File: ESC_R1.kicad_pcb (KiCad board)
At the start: 4 copper layers, 174 parts, among them J101 Conn_01x03_Pin, J102 Conn_01x02_Pin, J103 Conn_01x02_Pin, J104 Conn_01x02_Pin, J201 Conn_01x05_Pin, J202 SWD TagConnect, J301 Conn_01x04_Male, J401 USB_C_Receptacle, Q501 BSC072N08NS5, Q502 BSC072N08NS5, Q601 BSC072N08NS5, Q602 BSC072N08NS5, Q701 BSC072N08NS5, Q702 BSC072N08NS5, SW201 PTS810 SJK, U101 TPS54332D, U102 TPS561208D, U103 TLV75533PDBV, U201 STM32F446RETx, U301 TJA1441AT, U401 USBLC6-2SC6, U501 IR2181S, U502 AD8418, U601 IR2181S, U602 AD8418, U701 IR2181S, U702 AD8418, Y201 16MHz

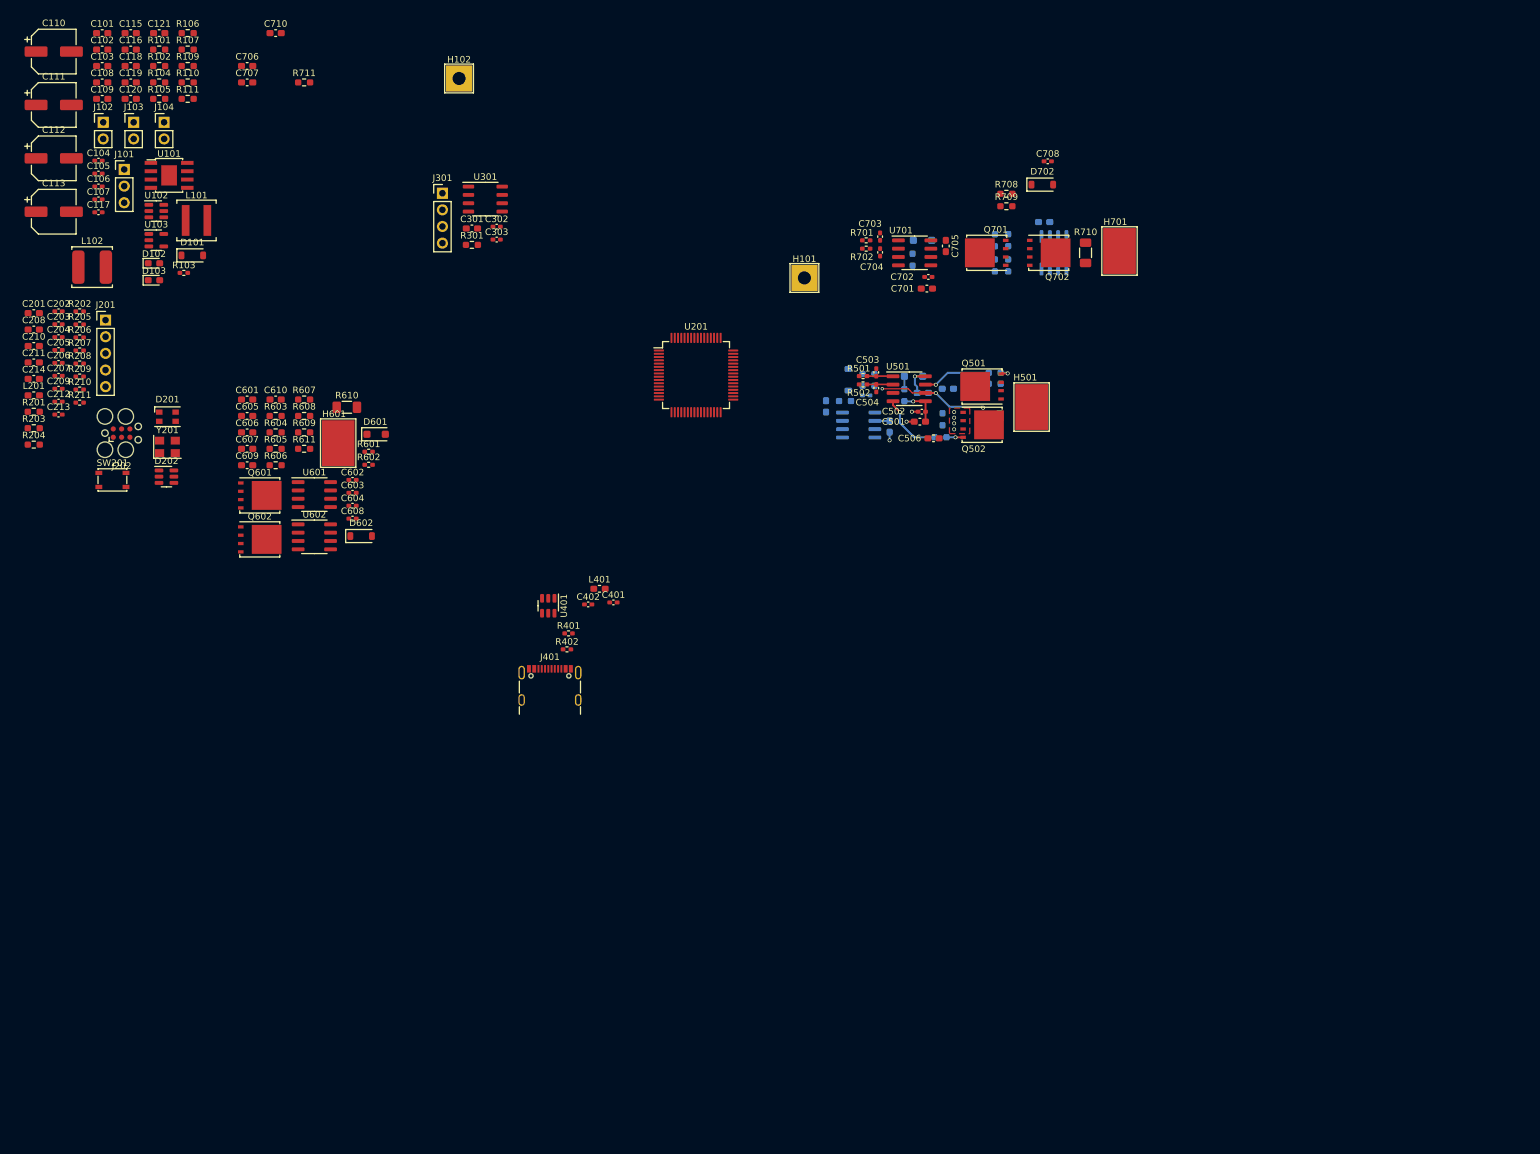
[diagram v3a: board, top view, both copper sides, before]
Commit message: feat: single phase, HSE, CAN routing and general layout
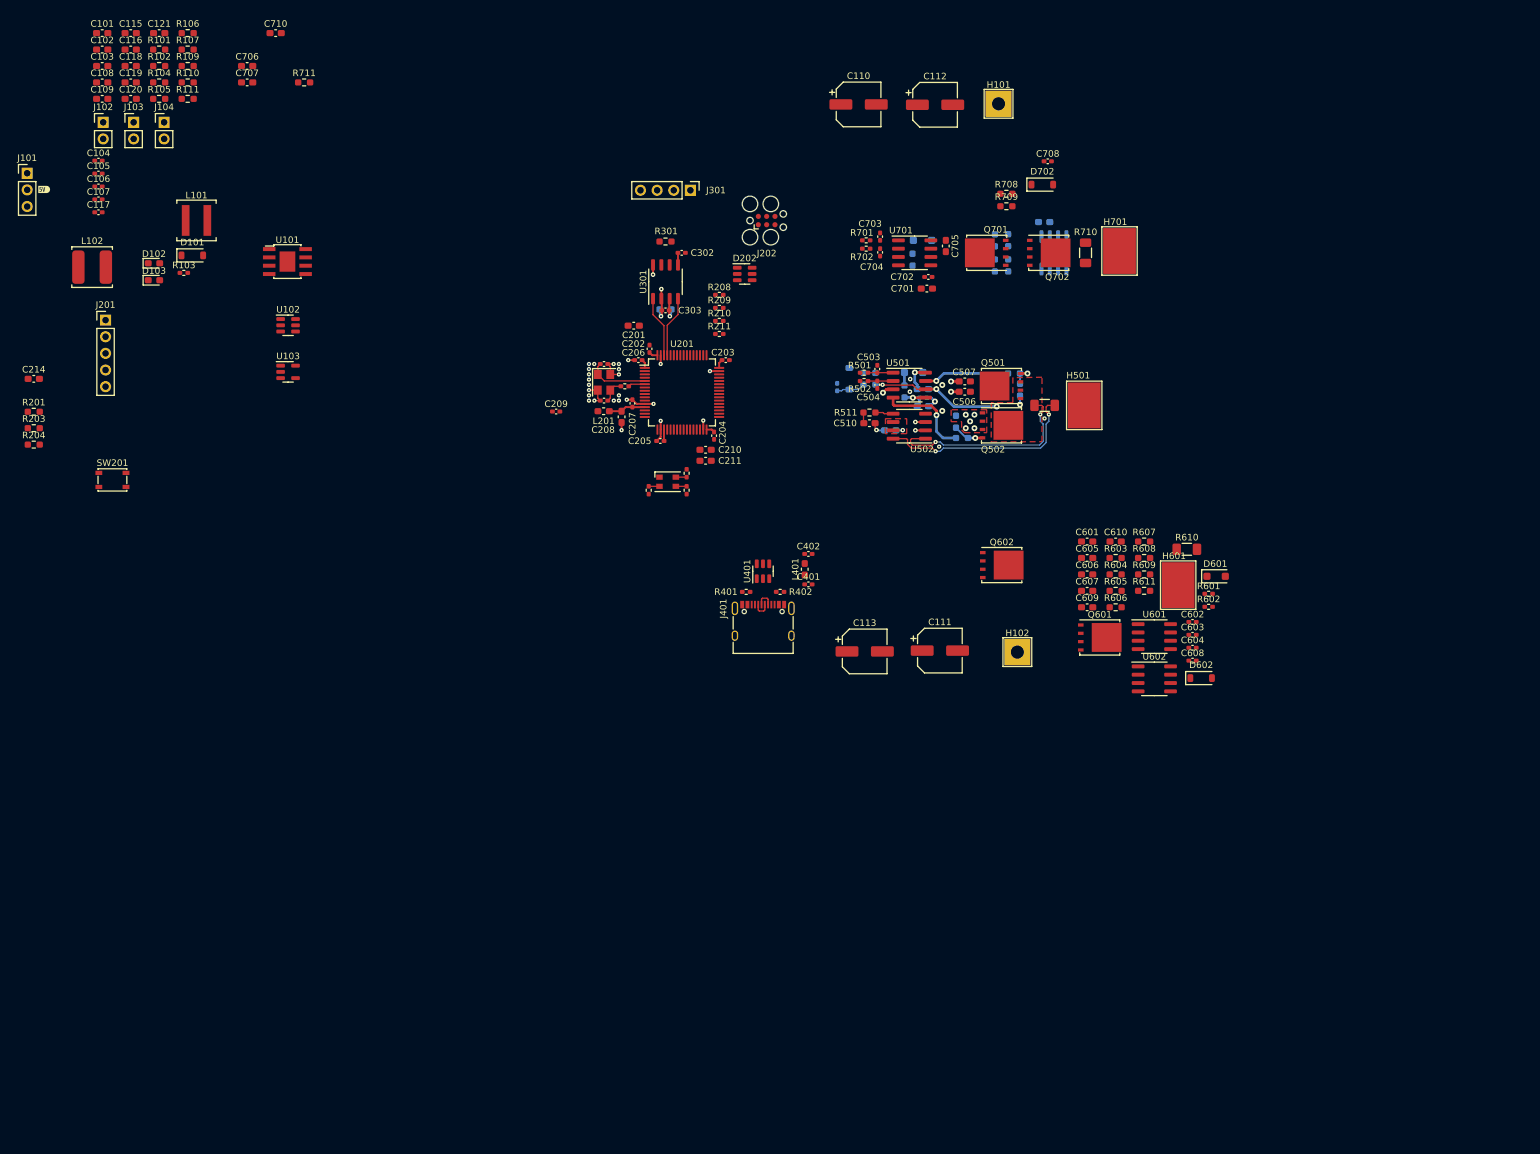
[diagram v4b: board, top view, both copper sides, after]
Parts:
- added kibuzzard-65860F08: G***, kibuzzard-65860F08, F.Cu at (18.3, 41.8)
- C301, C501, C502: moved to B.Cu
- C507, C510, R510, R511, U502: moved to F.Cu
- J401: footprint Connector_USB:USB_C_Receptacle_GCT_USB4105-xx-A_16P_TopMnt_Horizontal -> Connector_USB:USB_C_Receptacle_XKB_U262-16XN-4BVC11
- moved C111 158.9 mm to (155.0, 112.2)
- moved C113 140.8 mm to (143.6, 112.3)
- moved C112 134.8 mm to (154.3, 28.8)
- moved C601 130.1 mm to (177.5, 95.5)
- moved C602 130.1 mm to (193.6, 107.8)
- moved C603 130.1 mm to (193.6, 109.8)
- moved C604 130.1 mm to (193.6, 111.7)
- moved C605 130.1 mm to (177.5, 98.0)
- moved C606 130.1 mm to (177.5, 100.5)
- moved C607 130.1 mm to (177.5, 103.0)
- moved C608 130.1 mm to (193.6, 113.7)
- moved C609 130.1 mm to (177.5, 105.6)
- moved C610 130.1 mm to (181.9, 95.5)
- moved D601 130.1 mm to (197.2, 100.8)
- moved D602 130.1 mm to (194.9, 116.4)
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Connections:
- net /CAN/CANH renamed /CAN/CAN+
- net /CAN/CANL renamed /CAN/CAN-
- U401 pad 1: USB_D+ -> /USB/USB_CONN_D-
- U401 pad 3: USB_D- -> /USB/USB_CONN_D+
- U401 pad 4: /USB/USB_CONN_D- -> USB_D+
- U401 pad 6: /USB/USB_CONN_D+ -> USB_D-
- U502 pad 1: /3-Phase Bridge - Phase A/PHA_CIN- -> /3-Phase Bridge - Phase A/PHA_CIN+
- U502 pad 8: /3-Phase Bridge - Phase A/PHA_CIN+ -> /3-Phase Bridge - Phase A/PHA_CIN-
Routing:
- net GND: track 3.57 -> 41.1 mm, vias 3 -> 39
- net /3-Phase Bridge - Phase A/PHA_CIN+: track 17.7 -> 53.5 mm, vias 3 -> 6
- net /3-Phase Bridge - Phase A/PHA_CIN-: track 0.00 -> 32.3 mm, vias 0 -> 2
- net /MCU/HSE_IN: track 0.00 -> 9.34 mm
- net CAN_TXD: track 0.00 -> 9.33 mm
- net CAN_RXD: track 0.00 -> 9.32 mm
- net +3.3V: track 2.25 -> 10.0 mm, vias 0 -> 1
- net +3.3VA: track 0.00 -> 5.67 mm
- net /3-Phase Bridge - Phase A/PHA_LOUT: track 9.95 -> 14.6 mm
- net PHA_VSDIV: track 0.00 -> 4.41 mm
- net +5V: track 0.00 -> 3.87 mm, vias 0 -> 1
- net /MCU/XTAL_IN: track 0.00 -> 3.62 mm
- net /USB/USB_CONN_D+: track 0.00 -> 2.78 mm
- net /USB/USB_CONN_D-: track 0.00 -> 2.78 mm
- net PHA_C: track 0.00 -> 2.77 mm
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- added copper zone on F.Cu, net +3.3V
- added copper zone on F.Cu, net /3-Phase Bridge - Phase A/PHA_CIN+
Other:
- rule pad_to_mask_clearance: 0 -> 0.08

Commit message: feat: major circuit rework, style update and addition of a few extra subcomponents
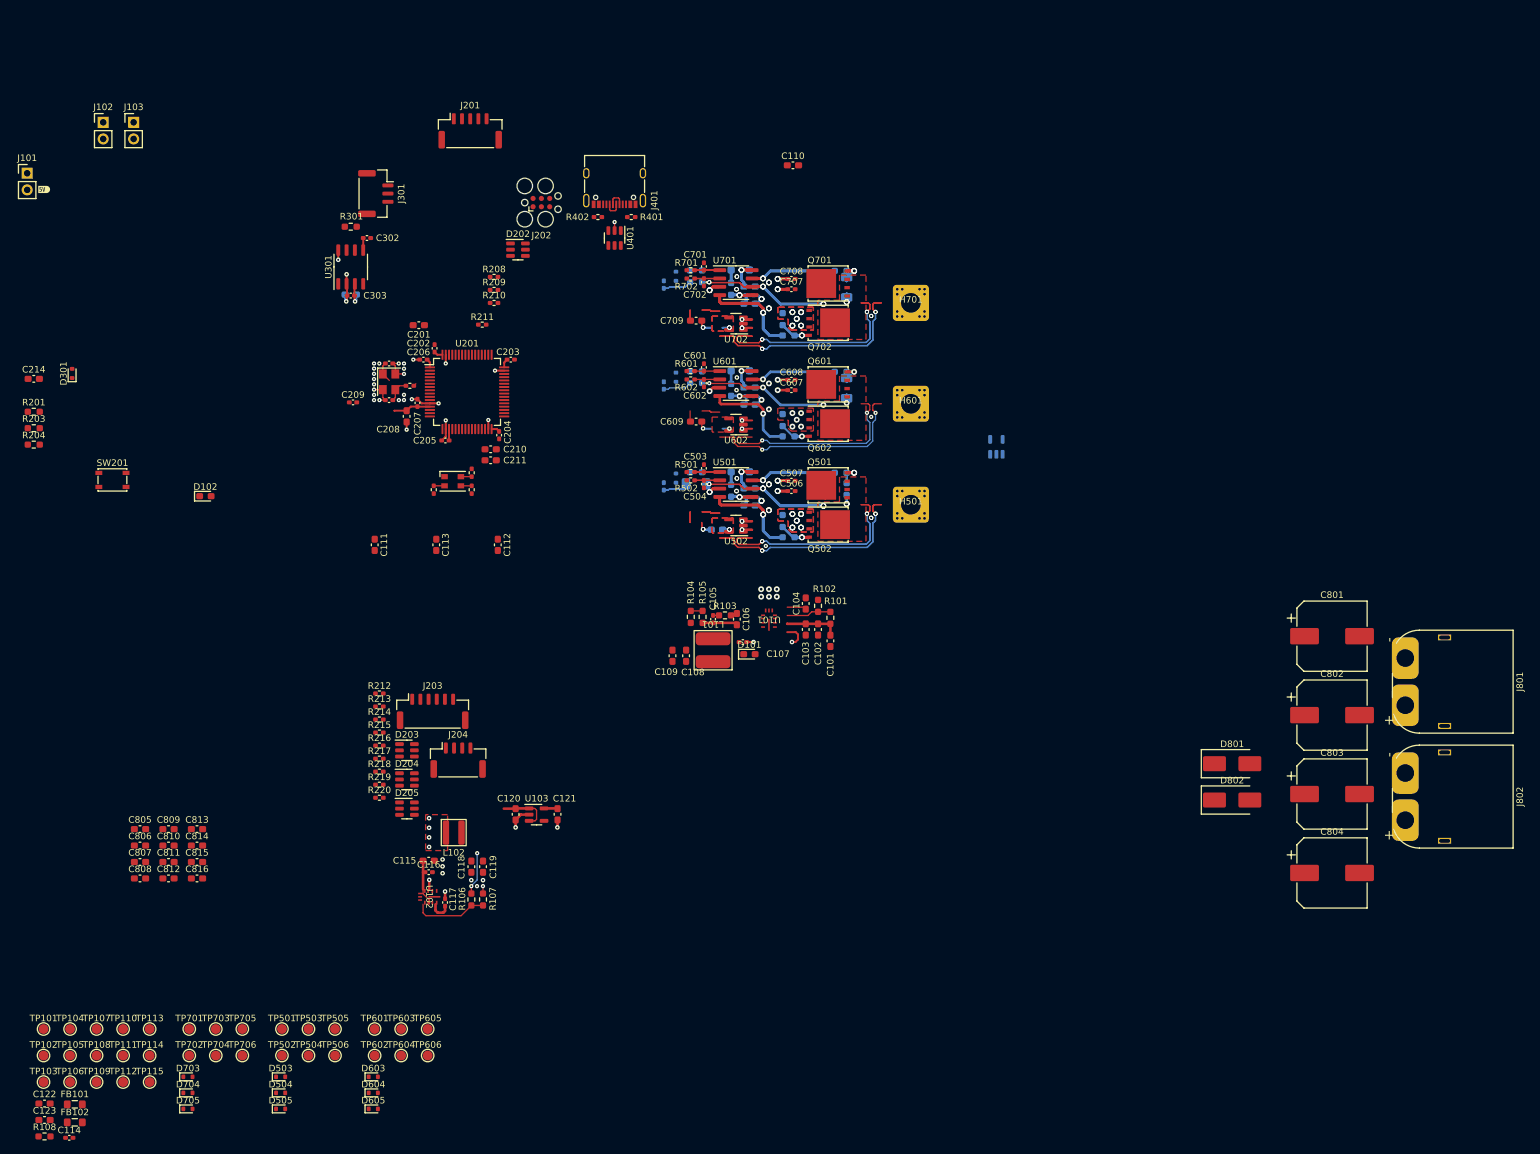
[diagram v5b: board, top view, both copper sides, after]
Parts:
- removed C401, C402: 100n, Capacitor_SMD:C_0402_1005Metric_Pad0.74x0.62mm_HandSolder
- removed C510, C610, C710: 10n, Capacitor_SMD:C_0603_1608Metric_Pad1.08x0.95mm_HandSolder
- removed D103: GREEN, LED_SMD:LED_0603_1608Metric_Pad1.05x0.95mm_HandSolder
- removed H101, H102: Pad, TestPoint:TestPoint_THTPad_4.0x4.0mm_Drill2.0mm
- removed J104: Conn_01x02_Pin, Connector_PinHeader_2.54mm:PinHeader_1x02_P2.54mm_Vertical
- removed L201, L401: WE742792625, Inductor_SMD:L_0603_1608Metric_Pad1.05x0.95mm_HandSolder
- removed R109: 0R5, Resistor_SMD:R_0603_1608Metric_Pad0.98x0.95mm_HandSolder
- removed R110: 1k, Resistor_SMD:R_0603_1608Metric_Pad0.98x0.95mm_HandSolder
- removed R111: 2k4, Resistor_SMD:R_0603_1608Metric_Pad0.98x0.95mm_HandSolder
- removed R510, R610, R710: 0.001, Resistor_SMD:R_1206_3216Metric_Pad1.30x1.75mm_HandSolder
- removed R511, R611, R711: 100, Resistor_SMD:R_0603_1608Metric_Pad0.98x0.95mm_HandSolder
- added C114: 100n 50V, Capacitor_SMD:C_0402_1005Metric_Pad0.74x0.62mm_HandSolder, F.Cu at (22.1, 186.6)
- added C122: 2u2 10V, Capacitor_SMD:C_0603_1608Metric_Pad1.08x0.95mm_HandSolder, F.Cu at (18.3, 181.3)
- added C123: 2u2 10V, Capacitor_SMD:C_0603_1608Metric_Pad1.08x0.95mm_HandSolder, F.Cu at (18.3, 183.8)
- added C801: 150u, Capacitor_SMD:CP_Elec_10x10.5, F.Cu at (214.9, 110.0)
- added C802: 150u, Capacitor_SMD:CP_Elec_10x10.5, F.Cu at (214.9, 122.0)
- added C803: 150u, Capacitor_SMD:CP_Elec_10x10.5, F.Cu at (214.9, 134.1)
- added C804: 150u, Capacitor_SMD:CP_Elec_10x10.5, F.Cu at (214.9, 146.1)
- added C805: 2u2 50V, Capacitor_SMD:C_0603_1608Metric_Pad1.08x0.95mm_HandSolder, F.Cu at (32.9, 139.4)
- added C806: 2u2 50V, Capacitor_SMD:C_0603_1608Metric_Pad1.08x0.95mm_HandSolder, F.Cu at (32.9, 141.9)
- added C807: 2u2 50V, Capacitor_SMD:C_0603_1608Metric_Pad1.08x0.95mm_HandSolder, F.Cu at (32.9, 144.4)
- added C808: 2u2 50V, Capacitor_SMD:C_0603_1608Metric_Pad1.08x0.95mm_HandSolder, F.Cu at (32.9, 147.0)
- added C809: 2u2 50V, Capacitor_SMD:C_0603_1608Metric_Pad1.08x0.95mm_HandSolder, F.Cu at (37.3, 139.4)
- added C810: 2u2 50V, Capacitor_SMD:C_0603_1608Metric_Pad1.08x0.95mm_HandSolder, F.Cu at (37.3, 141.9)
- added C811: 2u2 50V, Capacitor_SMD:C_0603_1608Metric_Pad1.08x0.95mm_HandSolder, F.Cu at (37.3, 144.4)
- added C812: 2u2 50V, Capacitor_SMD:C_0603_1608Metric_Pad1.08x0.95mm_HandSolder, F.Cu at (37.3, 147.0)
- added C813: 2u2 50V, Capacitor_SMD:C_0603_1608Metric_Pad1.08x0.95mm_HandSolder, F.Cu at (41.6, 139.4)
- added C814: 2u2 50V, Capacitor_SMD:C_0603_1608Metric_Pad1.08x0.95mm_HandSolder, F.Cu at (41.6, 141.9)
- added C815: 2u2 50V, Capacitor_SMD:C_0603_1608Metric_Pad1.08x0.95mm_HandSolder, F.Cu at (41.6, 144.4)
- added C816: 2u2 50V, Capacitor_SMD:C_0603_1608Metric_Pad1.08x0.95mm_HandSolder, F.Cu at (41.6, 147.0)
- added D203: ESDA6V1-5SC6, Package_TO_SOT_SMD:SOT-23-6, F.Cu at (73.7, 127.4)
- added D204: ESDA6V1-5SC6, Package_TO_SOT_SMD:SOT-23-6, F.Cu at (73.7, 131.8)
- added D205: ESDA6V1BC6, Package_TO_SOT_SMD:SOT-23-6, F.Cu at (73.7, 136.3)
- added D301: BAT41KFILM, Diode_SMD:D_SOD-523, F.Cu at (22.6, 69.8)
- added D503: BAT41KFILM, Diode_SMD:D_SOD-523, F.Cu at (54.4, 177.2)
- added D504: BAT41KFILM, Diode_SMD:D_SOD-523, F.Cu at (54.4, 179.7)
- added D505: BAT41KFILM, Diode_SMD:D_SOD-523, F.Cu at (54.4, 182.1)
- added D603: BAT41KFILM, Diode_SMD:D_SOD-523, F.Cu at (68.5, 177.2)
- added D604: BAT41KFILM, Diode_SMD:D_SOD-523, F.Cu at (68.5, 179.7)
- added D605: BAT41KFILM, Diode_SMD:D_SOD-523, F.Cu at (68.5, 182.1)
- added D703: BAT41KFILM, Diode_SMD:D_SOD-523, F.Cu at (40.2, 177.2)
- added D704: BAT41KFILM, Diode_SMD:D_SOD-523, F.Cu at (40.2, 179.7)
- added D705: BAT41KFILM, Diode_SMD:D_SOD-523, F.Cu at (40.2, 182.1)
- added D801: SMBJ33CA-13-F, Diode_SMD:D_SMB_Handsoldering, F.Cu at (199.7, 129.4)
- added D802: SMBJ33CA-13-F, Diode_SMD:D_SMB_Handsoldering, F.Cu at (199.7, 135.0)
- added FB101: 742792096, Inductor_SMD:L_0805_2012Metric_Pad1.05x1.20mm_HandSolder, F.Cu at (23.0, 181.4)
- added FB102: 742792096, Inductor_SMD:L_0805_2012Metric_Pad1.05x1.20mm_HandSolder, F.Cu at (23.0, 184.2)
- added J203: SM06B-GHS-TB, Connector_JST:JST_GH_SM06B-GHS-TB_1x06-1MP_P1.25mm_Horizontal, F.Cu at (77.6, 121.4)
- added J204: SM04B-GHS-TB, Connector_JST:JST_GH_SM04B-GHS-TB_1x04-1MP_P1.25mm_Horizontal, F.Cu at (81.5, 128.9)
- added J801: XT60PW-F, Connector_AMASS:XT60PW-M_1x02_P7.20mm_Horizontal_WP, F.Cu at (226.1, 113.3)
- added J802: XT60PW-M, Connector_AMASS:XT60PW-M_1x02_P7.20mm_Horizontal_WP, F.Cu at (226.1, 130.9)
- added R108: 1k, Resistor_SMD:R_0603_1608Metric_Pad0.98x0.95mm_HandSolder, F.Cu at (18.3, 186.3)
- added R212: 50, Resistor_SMD:R_0402_1005Metric_Pad0.72x0.64mm_HandSolder, F.Cu at (69.5, 118.7)
- added R213: 50, Resistor_SMD:R_0402_1005Metric_Pad0.72x0.64mm_HandSolder, F.Cu at (69.5, 120.7)
- added R214: 50, Resistor_SMD:R_0402_1005Metric_Pad0.72x0.64mm_HandSolder, F.Cu at (69.5, 122.7)
- added R215: 50, Resistor_SMD:R_0402_1005Metric_Pad0.72x0.64mm_HandSolder, F.Cu at (69.5, 124.7)
- added R216: 50, Resistor_SMD:R_0402_1005Metric_Pad0.72x0.64mm_HandSolder, F.Cu at (69.5, 126.7)
- added R217: 50, Resistor_SMD:R_0402_1005Metric_Pad0.72x0.64mm_HandSolder, F.Cu at (69.5, 128.7)
- added R218: 50, Resistor_SMD:R_0402_1005Metric_Pad0.72x0.64mm_HandSolder, F.Cu at (69.5, 130.7)
- added R219: 50, Resistor_SMD:R_0402_1005Metric_Pad0.72x0.64mm_HandSolder, F.Cu at (69.5, 132.6)
- added R220: 50, Resistor_SMD:R_0402_1005Metric_Pad0.72x0.64mm_HandSolder, F.Cu at (69.5, 134.6)
- added TP101: VBAT, TestPoint:TestPoint_Pad_D1.5mm, F.Cu at (18.2, 169.9)
- added TP102: VBAT, TestPoint:TestPoint_Pad_D1.5mm, F.Cu at (18.2, 174.0)
- added TP103: FILT_VIN_12V, TestPoint:TestPoint_Pad_D1.5mm, F.Cu at (18.2, 178.0)
- added TP104: FILT_VIN_5V, TestPoint:TestPoint_Pad_D1.5mm, F.Cu at (22.2, 169.9)
- added TP105: FILT_VIN_3V3A, TestPoint:TestPoint_Pad_D1.5mm, F.Cu at (22.2, 174.0)
- added TP106: FILT_VIN_3V3, TestPoint:TestPoint_Pad_D1.5mm, F.Cu at (22.2, 178.0)
- added TP107: 12V, TestPoint:TestPoint_Pad_D1.5mm, F.Cu at (26.3, 169.9)
- added TP108: 5V, TestPoint:TestPoint_Pad_D1.5mm, F.Cu at (26.3, 174.0)
- added TP109: 3V3, TestPoint:TestPoint_Pad_D1.5mm, F.Cu at (26.3, 178.0)
- added TP110: 3V3A, TestPoint:TestPoint_Pad_D1.5mm, F.Cu at (30.3, 169.9)
- added TP111: GND, TestPoint:TestPoint_Pad_D1.5mm, F.Cu at (30.3, 174.0)
- added TP112: GND, TestPoint:TestPoint_Pad_D1.5mm, F.Cu at (30.3, 178.0)
- added TP113: GND, TestPoint:TestPoint_Pad_D1.5mm, F.Cu at (34.4, 169.9)
- added TP114: GND, TestPoint:TestPoint_Pad_D1.5mm, F.Cu at (34.4, 174.0)
- added TP115: GND, TestPoint:TestPoint_Pad_D1.5mm, F.Cu at (34.4, 178.0)
- added TP501: PH_HIN, TestPoint:TestPoint_Pad_D1.5mm, F.Cu at (54.6, 169.9)
- added TP502: PH_LIN, TestPoint:TestPoint_Pad_D1.5mm, F.Cu at (54.6, 174.0)
- added TP503: PH_CURR_F, TestPoint:TestPoint_Pad_D1.5mm, F.Cu at (58.6, 169.9)
- added TP504: PH_VSDIV, TestPoint:TestPoint_Pad_D1.5mm, F.Cu at (58.6, 174.0)
- added TP505: GND, TestPoint:TestPoint_Pad_D1.5mm, F.Cu at (62.7, 169.9)
- added TP506: GND, TestPoint:TestPoint_Pad_D1.5mm, F.Cu at (62.7, 174.0)
- added TP601: PH_HIN, TestPoint:TestPoint_Pad_D1.5mm, F.Cu at (68.7, 169.9)
- added TP602: PH_LIN, TestPoint:TestPoint_Pad_D1.5mm, F.Cu at (68.7, 174.0)
- added TP603: PH_CURR_F, TestPoint:TestPoint_Pad_D1.5mm, F.Cu at (72.8, 169.9)
- added TP604: PH_VSDIV, TestPoint:TestPoint_Pad_D1.5mm, F.Cu at (72.8, 174.0)
- added TP605: GND, TestPoint:TestPoint_Pad_D1.5mm, F.Cu at (76.8, 169.9)
- added TP606: GND, TestPoint:TestPoint_Pad_D1.5mm, F.Cu at (76.8, 174.0)
- added TP701: PH_HIN, TestPoint:TestPoint_Pad_D1.5mm, F.Cu at (40.4, 169.9)
- added TP702: PH_LIN, TestPoint:TestPoint_Pad_D1.5mm, F.Cu at (40.4, 174.0)
- added TP703: PH_CURR_F, TestPoint:TestPoint_Pad_D1.5mm, F.Cu at (44.5, 169.9)
- added TP704: PH_VSDIV, TestPoint:TestPoint_Pad_D1.5mm, F.Cu at (44.5, 174.0)
- added TP705: GND, TestPoint:TestPoint_Pad_D1.5mm, F.Cu at (48.5, 169.9)
- added TP706: GND, TestPoint:TestPoint_Pad_D1.5mm, F.Cu at (48.5, 174.0)
- added U104: TLV75533PDBV, Package_TO_SOT_SMD:SOT-23-5, B.Cu at (163.7, 81.1)
- C101: value 22u -> 2u2 50V
- C102: value 10u -> 2u2 50V
- C103, C501: value 2u2 -> 2u2 50V
- C104: value 8n2 -> 2u2 50V; footprint Capacitor_SMD:C_0402_1005Metric_Pad0.74x0.62mm_HandSolder -> Capacitor_SMD:C_0603_1608Metric_Pad1.08x0.95mm_HandSolder
- C105: value 1n -> 100n 50V
- C106: value 6p8 -> 1u 10V; footprint Capacitor_SMD:C_0402_1005Metric_Pad0.74x0.62mm_HandSolder -> Capacitor_SMD:C_0603_1608Metric_Pad1.08x0.95mm_HandSolder
- C107, C502: value 100n -> 100n 50V
- C108, C109: value 22u -> 22u 25V
- C110, C111, C112, C113: value 100u -> 2u2 50V; footprint Capacitor_SMD:CP_Elec_6.3x7.7 -> Capacitor_SMD:C_0603_1608Metric_Pad1.08x0.95mm_HandSolder
- C115: value 22u -> 1u 10V
- C116: value 2u2 -> 100n 50V; footprint Capacitor_SMD:C_0603_1608Metric_Pad1.08x0.95mm_HandSolder -> Capacitor_SMD:C_0402_1005Metric_Pad0.74x0.62mm_HandSolder
- C117: value 100n -> 1.6p
- C118, C119: value 22u -> 10u 10V
- C120, C121, C201: value 10u -> 2u2 10V
- C208: value 1u -> 2u2 10V
- C210, C211, C301: value 2u2 -> 2u2 10V
- C214, C505: value 1u -> 1u 50V
- C506: value 22u -> DNP; footprint Capacitor_SMD:C_0603_1608Metric_Pad1.08x0.95mm_HandSolder -> Capacitor_SMD:C_0402_1005Metric_Pad0.74x0.62mm_HandSolder
- C507, C601, C607, C701, C707: value 2u2 -> 100n; footprint Capacitor_SMD:C_0603_1608Metric_Pad1.08x0.95mm_HandSolder -> Capacitor_SMD:C_0402_1005Metric_Pad0.74x0.62mm_HandSolder
- C508, C608, C708: value DNP -> 100n 50V
- C509, C609: value 2u2 -> 10n
- C603, C703: value 100n -> 2u2 50V; footprint Capacitor_SMD:C_0402_1005Metric_Pad0.74x0.62mm_HandSolder -> Capacitor_SMD:C_0603_1608Metric_Pad1.08x0.95mm_HandSolder; moved to B.Cu
- C604, C704: value 100n -> 100n 50V; moved to B.Cu
- C605, C705: value 1u -> 1u 50V; moved to B.Cu
- C606, C706: value 22u -> DNP; footprint Capacitor_SMD:C_0603_1608Metric_Pad1.08x0.95mm_HandSolder -> Capacitor_SMD:C_0402_1005Metric_Pad0.74x0.62mm_HandSolder; moved to B.Cu
- C709: value 2u2 -> 10n; moved to F.Cu
- D101: value B340LB-13-F -> GREEN; footprint Diode_SMD:D_SOD-123 -> LED_SMD:LED_0603_1608Metric_Pad1.05x0.95mm_HandSolder
- D202: value ESDA6V1-5SC6 -> ESDA6V1BC6
- D502: value MBR0530-TP -> BAT41KFILM; footprint Diode_SMD:D_SOD-123 -> Diode_SMD:D_SOD-523
- D601, R603, R604: moved to B.Cu
- D602, D702: value MBR0530-TP -> BAT41KFILM; footprint Diode_SMD:D_SOD-123 -> Diode_SMD:D_SOD-523; moved to B.Cu
- H501, H601, H701: footprint TestPoint:TestPoint_Pad_5.0x7.0mm -> TestPoint:Pad_5.5x5.5mm
- J101: value Conn_01x03_Pin -> Conn_01x02_Pin; footprint Connector_PinHeader_2.54mm:PinHeader_1x03_P2.54mm_Vertical -> Connector_PinHeader_2.54mm:PinHeader_1x02_P2.54mm_Vertical
- J201: value Conn_01x05_Pin -> SM05B-GHS-TB; footprint Connector_PinHeader_2.54mm:PinHeader_1x05_P2.54mm_Vertical -> Connector_JST:JST_GH_SM05B-GHS-TB_1x05-1MP_P1.25mm_Horizontal
- J301: value Conn_01x04_Male -> SM03B-GHS-TB; footprint Connector_PinHeader_2.54mm:PinHeader_1x04_P2.54mm_Vertical -> Connector_JST:JST_GH_SM03B-GHS-TB_1x03-1MP_P1.25mm_Horizontal
- J401: value USB_C_Receptacle -> USB_C_Receptacle_USB2.0
- L101: value 8u2 -> 74408943150; footprint Inductor_SMD:L_Coilcraft_XAL5050-XXX -> Inductor_SMD_Wurth:74408943150
- L102: value 4u7 -> 74438357082; footprint Inductor_SMD:L_TDK_VLS6045EX_VLS6045AF -> Inductor_SMD_Wurth:74438357082
- R101: value 681k -> 100k
- R102: value 82k5 -> 9.09k
- R103: value 56k2 -> 54k9; footprint Resistor_SMD:R_0402_1005Metric_Pad0.72x0.64mm_HandSolder -> Resistor_SMD:R_0603_1608Metric_Pad0.98x0.95mm_HandSolder
- R104: value 10k2 -> 10k
- R105: value 732 -> 0R5
- R106: value 54k9 -> 0R5
- R107: value 10k -> 2k4
- R505, R705: value 10k -> 4R7
- R506, R706: value 4R7 -> 2k2
- R507, R707: value 10k -> 17k8
- R508: value 17k8 -> 0.001; footprint Resistor_SMD:R_0603_1608Metric_Pad0.98x0.95mm_HandSolder -> Resistor_SMD:R_1206_3216Metric_Pad1.30x1.75mm_HandSolder
- R509: value 2k2 -> 100
- R605: value 10k -> 4R7; moved to B.Cu
- R606: value 4R7 -> 2k2; moved to B.Cu
- R607: value 10k -> 17k8; moved to B.Cu
- R608, R708: value 17k8 -> 0.001; footprint Resistor_SMD:R_0603_1608Metric_Pad0.98x0.95mm_HandSolder -> Resistor_SMD:R_1206_3216Metric_Pad1.30x1.75mm_HandSolder; moved to B.Cu
- R609, R709: value 2k2 -> 100; moved to B.Cu
- U101: value TPS54332D -> LMR36006; footprint Package_SO:TI_SO-PowerPAD-8 -> LMR36006:RNX0012B
- U102: value TPS561208D -> LMR36006; footprint Package_TO_SOT_SMD:SOT-23-6 -> LMR36006:RNX0012B
- U501, U601, U701: value IR2181S -> IR2171S
- U502, U602: value AD8418 -> INA180B2; footprint Package_SO:SOIC-8_3.9x4.9mm_P1.27mm -> Package_TO_SOT_SMD:SOT-23-5
- U702: value AD8418 -> INA180B2; footprint Package_SO:SOIC-8_3.9x4.9mm_P1.27mm -> Package_TO_SOT_SMD:SOT-23-5; moved to F.Cu
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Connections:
- net /3-Phase Bridge - Phase A/PHA_IR_HIN renamed /[5] 3-Phase Bridge - Phase A/PH_IR_HIN
- net /3-Phase Bridge - Phase A/PHA_IR_LIN renamed /[5] 3-Phase Bridge - Phase A/PH_IR_LIN
- net /3-Phase Bridge - Phase A/PHA_VB renamed /[5] 3-Phase Bridge - Phase A/PH_VB
- net /3-Phase Bridge - Phase A/PHA_VRD renamed /[5] 3-Phase Bridge - Phase A/PH_VRD
- net /3-Phase Bridge - Phase B/PHB_VB renamed /[6] 3-Phase Bridge - Phase B/PH_VB
- net /3-Phase Bridge - Phase B/PHB_VRD renamed /[6] 3-Phase Bridge - Phase B/PH_VRD
- net /3-Phase Bridge - Phase C/PHC_VB renamed /[7] 3-Phase Bridge - Phase C/PH_VB
- net /3-Phase Bridge - Phase C/PHC_VRD renamed /[7] 3-Phase Bridge - Phase C/PH_VRD
- net /CAN/CAN- renamed /[3] CAN/CAN-
- net /MCU/BOOT0 renamed /[2] MCU/BOOT0
- net /MCU/HSE_IN renamed /[2] MCU/HSE_IN
- net /MCU/HSE_OUT renamed /[2] MCU/HSE_OUT
- net /MCU/LED_B renamed /[2] MCU/LED_B
- net /MCU/LED_G renamed /[2] MCU/LED_G
- net /MCU/LED_R renamed /[2] MCU/LED_R
- net /MCU/RGB_B renamed /[2] MCU/RGB_B
- net /MCU/RGB_G renamed /[2] MCU/RGB_G
- net /MCU/RGB_R renamed /[2] MCU/RGB_R
- net /MCU/TEMP renamed /[2] MCU/TEMP
- net /MCU/XTAL_IN renamed /[2] MCU/XTAL_IN
- net /USB/USB_CC1 renamed /[4] USB/USB_CC1
- net /USB/USB_CC2 renamed /[4] USB/USB_CC2
- net /USB/USB_CONN_D+ renamed /[4] USB/USB_CONN_D+
- net /USB/USB_CONN_D- renamed /[4] USB/USB_CONN_D-
- net /USB/USB_VBUS renamed /[4] USB/USB_VBUS
- net PHA_HIN renamed /[2] MCU/PHA_HIN
- net PHA_LIN renamed /[2] MCU/PHA_LIN
- net PHB_HIN renamed /[2] MCU/PHB_HIN
- net PHB_LIN renamed /[2] MCU/PHB_LIN
- net PHC_HIN renamed /[2] MCU/PHC_HIN
- net PHC_LIN renamed /[2] MCU/PHC_LIN
- C102 pad 1: +BATT -> /[1] Power Supply/FILT_VIN_12V
- C103 pad 1: +BATT -> /[1] Power Supply/FILT_VIN_12V
- C104 pad 1: /Power Supply/S12_SS -> /[1] Power Supply/FILT_VIN_12V
- C105 pad 1: Net-(C105-Pad1) -> /[1] Power Supply/FILT_VIN_12V
- C106 pad 1: /Power Supply/S12_COMP -> Net-(U101-VCC)
- C107 pad 1: /Power Supply/S12_BOOT -> /[1] Power Supply/VSW_12V
- C107 pad 2: /Power Supply/S12_PH -> Net-(U101-BOOT)
- C110 pad 1: +12V -> +BATT
- C111 pad 1: +BATT -> /[1] Power Supply/FILT_VIN_5V
- C112 pad 1: +BATT -> /[1] Power Supply/FILT_VIN_5V
- C113 pad 1: +BATT -> /[1] Power Supply/FILT_VIN_5V
- C115 pad 1: +12V -> Net-(U102-VCC)
- C116 pad 1: +12V -> /[1] Power Supply/VSW_5V
- C116 pad 2: GND -> Net-(U102-BOOT)
- C117 pad 1: /Power Supply/S5_BTS -> /[1] Power Supply/VFB_5V
- C117 pad 2: /Power Supply/S5_SW -> +5V
- C118 pad 1: +5VP -> +5V
- C119 pad 1: +5VP -> +5V
- C120 pad 1: /Power Supply/5V_FILT -> /[1] Power Supply/FILT_VIN_3V3A
- C121 pad 1: +3.3V -> +3.3VA
- C209 pad 1: /MCU/NRST -> /[2] MCU/NRST
- C210 pad 1: GND -> /[2] MCU/VCAP1
- C210 pad 2: /MCU/VCAP1 -> GND
- C211 pad 1: GND -> /[2] MCU/VCAP1
- C211 pad 2: /MCU/VCAP1 -> GND
- C501 pad 1: GND -> +12V
- C501 pad 2: +12V -> GND
- C505 pad 2: /3-Phase Bridge - Phase A/PHA_CIN+ -> /[5] 3-Phase Bridge - Phase A/PH_VS
- C506 pad 2: +BATT -> /[2] MCU/PHA_VSDIV
- C507 pad 1: GND -> +3.3VA
- C507 pad 2: +BATT -> GND
- C508 pad 1: GND -> +BATT
- C508 pad 2: PHA_VSDIV -> /[5] 3-Phase Bridge - Phase A/PH_CIN+
- C509 pad 2: +3.3V -> /[2] MCU/PHA_CURR_FILT
- C601 pad 1: GND -> /[6] 3-Phase Bridge - Phase B/PH_IR_HIN
- C601 pad 2: +12V -> GND
- C602 pad 1: GND -> /[6] 3-Phase Bridge - Phase B/PH_IR_LIN
- C602 pad 2: +12V -> GND
- C603 pad 1: /3-Phase Bridge - Phase B/PHB_IR_HIN -> +12V
- C604 pad 1: /3-Phase Bridge - Phase B/PHB_IR_LIN -> GND
- C604 pad 2: GND -> +12V
- C605 pad 2: /3-Phase Bridge - Phase B/PHB_VS -> /[6] 3-Phase Bridge - Phase B/PH_VS
- C606 pad 2: +BATT -> /[2] MCU/PHB_VSDIV
- C607 pad 1: GND -> +3.3VA
- C607 pad 2: +BATT -> GND
- C608 pad 1: GND -> +BATT
- C608 pad 2: PHB_VSDIV -> /[6] 3-Phase Bridge - Phase B/PH_CIN+
- C609 pad 2: +3.3V -> /[2] MCU/PHB_CURR_FILT
- C701 pad 1: GND -> /[7] 3-Phase Bridge - Phase C/PH_IR_HIN
- C701 pad 2: +12V -> GND
- C702 pad 1: GND -> /[7] 3-Phase Bridge - Phase C/PH_IR_LIN
- C702 pad 2: +12V -> GND
- C703 pad 1: /3-Phase Bridge - Phase C/PHC_IR_HIN -> +12V
- C704 pad 1: /3-Phase Bridge - Phase C/PHC_IR_LIN -> GND
- C704 pad 2: GND -> +12V
- C705 pad 2: /3-Phase Bridge - Phase C/PHC_VS -> /[7] 3-Phase Bridge - Phase C/PH_VS
- C706 pad 2: +BATT -> /[2] MCU/PHC_VSDIV
- C707 pad 1: GND -> +3.3VA
- C707 pad 2: +BATT -> GND
- C708 pad 1: GND -> +BATT
- C708 pad 2: PHC_VSDIV -> /[7] 3-Phase Bridge - Phase C/PH_CIN+
- C709 pad 2: +3.3V -> /[2] MCU/PHC_CURR_FILT
- D101 pad 1: /Power Supply/S12_PH -> /[1] Power Supply/5V_LED_K
- D101 pad 2: GND -> +5V
- D102 pad 1: /Power Supply/5V_LED_K -> /[1] Power Supply/3V3_LED_K
- D102 pad 2: +5VP -> +3.3V
- D202 pad 1: /MCU/TC_SYS_SWO -> Net-(D202-CH1)
- D202 pad 3: /MCU/TC_SYS_SWDIO -> Net-(D202-CH2)
- D202 pad 4: /MCU/TC_SYS_SWDCLK -> Net-(D202-CH3)
- D202 pad 5: /MCU/TC_NRST -> GND
- D502 pad 1: +3.3V -> /[5] 3-Phase Bridge - Phase A/PH_HOUT
- D502 pad 2: PHA_VSDIV -> /[5] 3-Phase Bridge - Phase A/PH_HOUT_G
- D602 pad 1: +3.3V -> /[6] 3-Phase Bridge - Phase B/PH_HOUT
- D602 pad 2: PHB_VSDIV -> /[6] 3-Phase Bridge - Phase B/PH_HOUT_G
- D702 pad 1: +3.3V -> /[7] 3-Phase Bridge - Phase C/PH_HOUT
- D702 pad 2: PHC_VSDIV -> /[7] 3-Phase Bridge - Phase C/PH_HOUT_G
- H501 pad 1: /3-Phase Bridge - Phase A/PHA_CIN- -> /[5] 3-Phase Bridge - Phase A/PH_VS
- H601 pad 1: /3-Phase Bridge - Phase B/PHB_PAD -> /[6] 3-Phase Bridge - Phase B/PH_VS
- H701 pad 1: /3-Phase Bridge - Phase C/PHC_PAD -> /[7] 3-Phase Bridge - Phase C/PH_VS
- J101 pad 1: +5VP -> GND
- J101 pad 2: +5V -> +12V
- J102 pad 2: +12V -> +5V
- J103 pad 2: +5V -> +3.3V
- J201 pad 1: /MCU/ENC_A -> +3.3V
- J201 pad 2: /MCU/ENC_B -> Net-(D202-CH3)
- J201 pad 3: /MCU/ENC_Z -> Net-(D202-CH2)
- J201 pad 4: GND -> Net-(D202-CH1)
- J201 pad 5: +3.3V -> GND
- J202 pad 2: /MCU/TC_SYS_SWDIO -> /[2] MCU/TC_SYS_SWDIO
- J202 pad 3: /MCU/TC_NRST -> /[2] MCU/TC_NRST
- J202 pad 4: /MCU/TC_SYS_SWDCLK -> /[2] MCU/TC_SYS_SWDCLK
- J202 pad 6: /MCU/TC_SYS_SWO -> /[2] MCU/TC_SYS_SWO
- J301 pad 1: GND -> /[3] CAN/CAN+
- J301 pad 3: /CAN/CAN+ -> GND
- L101 pad 1: /Power Supply/S12_PH -> /[1] Power Supply/VSW_12V
- L102 pad 1: /Power Supply/S5_SW -> /[1] Power Supply/VSW_5V
- L102 pad 2: +5VP -> +5V
- Q501 pad 1: /3-Phase Bridge - Phase A/PHA_CIN+ -> /[5] 3-Phase Bridge - Phase A/PH_VS
- Q501 pad 2: /3-Phase Bridge - Phase A/PHA_CIN+ -> /[5] 3-Phase Bridge - Phase A/PH_VS
- Q501 pad 3: /3-Phase Bridge - Phase A/PHA_CIN+ -> /[5] 3-Phase Bridge - Phase A/PH_VS
- Q501 pad 4: /3-Phase Bridge - Phase A/PHA_HOUT_G -> /[5] 3-Phase Bridge - Phase A/PH_HOUT_G
- Q502 pad 1: GND -> /[5] 3-Phase Bridge - Phase A/PH_CIN+
- Q502 pad 2: GND -> /[5] 3-Phase Bridge - Phase A/PH_CIN+
- Q502 pad 3: GND -> /[5] 3-Phase Bridge - Phase A/PH_CIN+
- Q502 pad 4: /3-Phase Bridge - Phase A/PHA_LOUT_G -> /[5] 3-Phase Bridge - Phase A/PH_LOUT_G
- Q502 pad 5: /3-Phase Bridge - Phase A/PHA_CIN+ -> /[5] 3-Phase Bridge - Phase A/PH_VS
- Q601 pad 1: /3-Phase Bridge - Phase B/PHB_VS -> /[6] 3-Phase Bridge - Phase B/PH_VS
- Q601 pad 2: /3-Phase Bridge - Phase B/PHB_VS -> /[6] 3-Phase Bridge - Phase B/PH_VS
- Q601 pad 3: /3-Phase Bridge - Phase B/PHB_VS -> /[6] 3-Phase Bridge - Phase B/PH_VS
- Q601 pad 4: /3-Phase Bridge - Phase B/PHB_HOUT_G -> /[6] 3-Phase Bridge - Phase B/PH_HOUT_G
- Q602 pad 1: GND -> /[6] 3-Phase Bridge - Phase B/PH_CIN+
- Q602 pad 2: GND -> /[6] 3-Phase Bridge - Phase B/PH_CIN+
- Q602 pad 3: GND -> /[6] 3-Phase Bridge - Phase B/PH_CIN+
- Q602 pad 4: /3-Phase Bridge - Phase B/PHB_LOUT_G -> /[6] 3-Phase Bridge - Phase B/PH_LOUT_G
- Q602 pad 5: /3-Phase Bridge - Phase B/PHB_VS -> /[6] 3-Phase Bridge - Phase B/PH_VS
- Q701 pad 1: /3-Phase Bridge - Phase C/PHC_VS -> /[7] 3-Phase Bridge - Phase C/PH_VS
- Q701 pad 2: /3-Phase Bridge - Phase C/PHC_VS -> /[7] 3-Phase Bridge - Phase C/PH_VS
- Q701 pad 3: /3-Phase Bridge - Phase C/PHC_VS -> /[7] 3-Phase Bridge - Phase C/PH_VS
- Q701 pad 4: /3-Phase Bridge - Phase C/PHC_HOUT_G -> /[7] 3-Phase Bridge - Phase C/PH_HOUT_G
- Q702 pad 1: GND -> /[7] 3-Phase Bridge - Phase C/PH_CIN+
- Q702 pad 2: GND -> /[7] 3-Phase Bridge - Phase C/PH_CIN+
- Q702 pad 3: GND -> /[7] 3-Phase Bridge - Phase C/PH_CIN+
- Q702 pad 4: /3-Phase Bridge - Phase C/PHC_LOUT_G -> /[7] 3-Phase Bridge - Phase C/PH_LOUT_G
- Q702 pad 5: /3-Phase Bridge - Phase C/PHC_VS -> /[7] 3-Phase Bridge - Phase C/PH_VS
- R101 pad 1: /Power Supply/S12_EN -> /[1] Power Supply/VFB_12V
- R101 pad 2: +BATT -> +12V
- R102 pad 2: /Power Supply/S12_EN -> /[1] Power Supply/VFB_12V
- R103 pad 1: Net-(C105-Pad1) -> /[1] Power Supply/VFB_5V
- R103 pad 2: /Power Supply/S12_COMP -> +5V
- R104 pad 1: S12_VFB -> GND
- R104 pad 2: +12V -> /[1] Power Supply/VFB_5V
- R105 pad 1: GND -> /[1] Power Supply/FILT_VIN_3V3A
- R105 pad 2: S12_VFB -> +5V
- R106 pad 1: /Power Supply/S5_VFB -> /[1] Power Supply/FILT_VIN_3V3
- R106 pad 2: +5VP -> +5V
- R107 pad 2: /Power Supply/S5_VFB -> /[1] Power Supply/5V_LED_K
- R208 pad 1: /MCU/NRST -> /[2] MCU/ENC_Z
- R208 pad 2: /MCU/TC_NRST -> Net-(D202-CH3)
- R209 pad 1: /MCU/SYS_SWDCLK -> /[2] MCU/ENC_B
- R209 pad 2: /MCU/TC_SYS_SWDCLK -> Net-(D202-CH2)
- R210 pad 1: /MCU/SYS_SWDIO -> /[2] MCU/ENC_A
- R210 pad 2: /MCU/TC_SYS_SWDIO -> Net-(D202-CH1)
- R211 pad 1: /MCU/SYS_SWO -> /[2] MCU/NRST
- R211 pad 2: /MCU/TC_SYS_SWO -> /[2] MCU/TC_NRST
- R301 pad 2: /CAN/CAN+ -> /[3] CAN/CAN+
- R504 pad 1: /3-Phase Bridge - Phase A/PHA_HOUT -> /[5] 3-Phase Bridge - Phase A/PH_HOUT
- R504 pad 2: /3-Phase Bridge - Phase A/PHA_HOUT_G -> /[5] 3-Phase Bridge - Phase A/PH_HOUT_G
- R505 pad 1: /3-Phase Bridge - Phase A/PHA_CIN+ -> /[5] 3-Phase Bridge - Phase A/PH_LOUT
- R505 pad 2: /3-Phase Bridge - Phase A/PHA_HOUT_G -> /[5] 3-Phase Bridge - Phase A/PH_LOUT_G
- R506 pad 1: /3-Phase Bridge - Phase A/PHA_LOUT -> /[2] MCU/PHA_VSDIV
- R506 pad 2: /3-Phase Bridge - Phase A/PHA_LOUT_G -> GND
- R507 pad 1: GND -> /[2] MCU/PHA_VSDIV
- R507 pad 2: /3-Phase Bridge - Phase A/PHA_LOUT_G -> /[5] 3-Phase Bridge - Phase A/PH_VS
- R508 pad 1: PHA_VSDIV -> GND
- R508 pad 2: /3-Phase Bridge - Phase A/PHA_CIN+ -> /[5] 3-Phase Bridge - Phase A/PH_CIN+
- R509 pad 1: PHA_VSDIV -> /[2] MCU/PHA_CURR_FILT
- R509 pad 2: GND -> /[5] 3-Phase Bridge - Phase A/PH_CURR
- R601 pad 2: /3-Phase Bridge - Phase B/PHB_IR_HIN -> /[6] 3-Phase Bridge - Phase B/PH_IR_HIN
- R602 pad 2: /3-Phase Bridge - Phase B/PHB_IR_LIN -> /[6] 3-Phase Bridge - Phase B/PH_IR_LIN
- R604 pad 1: /3-Phase Bridge - Phase B/PHB_HOUT -> /[6] 3-Phase Bridge - Phase B/PH_HOUT
- R604 pad 2: /3-Phase Bridge - Phase B/PHB_HOUT_G -> /[6] 3-Phase Bridge - Phase B/PH_HOUT_G
- R605 pad 1: /3-Phase Bridge - Phase B/PHB_VS -> /[6] 3-Phase Bridge - Phase B/PH_LOUT
- R605 pad 2: /3-Phase Bridge - Phase B/PHB_HOUT_G -> /[6] 3-Phase Bridge - Phase B/PH_LOUT_G
- R606 pad 1: /3-Phase Bridge - Phase B/PHB_LOUT -> /[2] MCU/PHB_VSDIV
- R606 pad 2: /3-Phase Bridge - Phase B/PHB_LOUT_G -> GND
- R607 pad 1: GND -> /[2] MCU/PHB_VSDIV
- R607 pad 2: /3-Phase Bridge - Phase B/PHB_LOUT_G -> /[6] 3-Phase Bridge - Phase B/PH_VS
- R608 pad 1: PHB_VSDIV -> GND
- R608 pad 2: /3-Phase Bridge - Phase B/PHB_VS -> /[6] 3-Phase Bridge - Phase B/PH_CIN+
- R609 pad 1: PHB_VSDIV -> /[2] MCU/PHB_CURR_FILT
- R609 pad 2: GND -> /[6] 3-Phase Bridge - Phase B/PH_CURR
- R701 pad 2: /3-Phase Bridge - Phase C/PHC_IR_HIN -> /[7] 3-Phase Bridge - Phase C/PH_IR_HIN
- R702 pad 2: /3-Phase Bridge - Phase C/PHC_IR_LIN -> /[7] 3-Phase Bridge - Phase C/PH_IR_LIN
- R704 pad 1: /3-Phase Bridge - Phase C/PHC_HOUT -> /[7] 3-Phase Bridge - Phase C/PH_HOUT
- R704 pad 2: /3-Phase Bridge - Phase C/PHC_HOUT_G -> /[7] 3-Phase Bridge - Phase C/PH_HOUT_G
- R705 pad 1: /3-Phase Bridge - Phase C/PHC_VS -> /[7] 3-Phase Bridge - Phase C/PH_LOUT
- R705 pad 2: /3-Phase Bridge - Phase C/PHC_HOUT_G -> /[7] 3-Phase Bridge - Phase C/PH_LOUT_G
- R706 pad 1: /3-Phase Bridge - Phase C/PHC_LOUT -> /[2] MCU/PHC_VSDIV
- R706 pad 2: /3-Phase Bridge - Phase C/PHC_LOUT_G -> GND
- R707 pad 1: GND -> /[2] MCU/PHC_VSDIV
- R707 pad 2: /3-Phase Bridge - Phase C/PHC_LOUT_G -> /[7] 3-Phase Bridge - Phase C/PH_VS
- R708 pad 1: PHC_VSDIV -> GND
- R708 pad 2: /3-Phase Bridge - Phase C/PHC_VS -> /[7] 3-Phase Bridge - Phase C/PH_CIN+
- R709 pad 1: PHC_VSDIV -> /[2] MCU/PHC_CURR_FILT
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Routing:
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- added copper zone on F.Cu, net /[1] Power Supply/FILT_VIN_5V
- added copper zone on In1.Cu, net /[1] Power Supply/FILT_VIN_5V
- added copper zone on F.Cu, net /[5] 3-Phase Bridge - Phase A/PH_CIN+
- added copper zone on F.Cu, net /[6] 3-Phase Bridge - Phase B/PH_CIN+
- added copper zone on F.Cu, net /[7] 3-Phase Bridge - Phase C/PH_CIN+
- added copper zone on In1.Cu, net unconnected-(U101-PG-Pad8)
- removed copper zone on F.Cu, net /3-Phase Bridge - Phase A/PHA_CIN+

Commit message: feat: component placement, again
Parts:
- C101, C102, C103, C104, C110, C111, C112, C113, C501, C603, C703, C808, C809, C810, C811, C812, C813, C815, C816: footprint Capacitor_SMD:C_0603_1608Metric_Pad1.08x0.95mm_HandSolder -> Capacitor_SMD:C_0805_2012Metric_Pad1.18x1.45mm_HandSolder
- C508, C608, C708: footprint Capacitor_SMD:C_0402_1005Metric_Pad0.74x0.62mm_HandSolder -> Capacitor_SMD:C_0805_2012Metric_Pad1.18x1.45mm_HandSolder
- C805, C806, C807, C814: footprint Capacitor_SMD:C_0603_1608Metric_Pad1.08x0.95mm_HandSolder -> Capacitor_SMD:C_0805_2012Metric_Pad1.18x1.45mm_HandSolder; moved to B.Cu
- D702, R704, R705, R708: moved to F.Cu
- J801: footprint Connector_AMASS:XT60PW-M_1x02_P7.20mm_Horizontal_WP -> Connector_AMASS:XT60PW-F_1x02_P7.20mm_Horizontal; moved to B.Cu
- J802: moved to B.Cu
- moved D704 202.9 mm to (203.1, 58.7), turned to -90 degrees
- moved C807 197.5 mm to (200.6, 40.0)
- moved C806 197.3 mm to (200.6, 37.9)
- moved C805 197.2 mm to (200.6, 35.7)
- moved D703 196.4 mm to (194.9, 56.3)
- moved C814 192.4 mm to (200.6, 33.5)
- moved C813 185.9 mm to (202.8, 46.9), turned to 90 degrees
- moved D705 184.9 mm to (178.1, 59.0)
- moved C815 97.4 mm to (138.8, 137.5)
- moved C816 97.4 mm to (138.8, 140.0)
- moved C808 96.3 mm to (128.9, 140.0)
- moved C809 96.3 mm to (133.3, 132.5)
- moved C810 96.3 mm to (133.3, 135.0)
- moved C811 96.3 mm to (133.3, 137.5)
- moved C812 96.3 mm to (133.3, 140.0)
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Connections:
- U502 pad 1: /[5] 3-Phase Bridge - Phase A/PH_CURR -> /[5] 3-Phase Bridge - Phase A/PH_CIN+
- U502 pad 3: /[5] 3-Phase Bridge - Phase A/PH_CIN+ -> GND
- U502 pad 4: GND -> /[5] 3-Phase Bridge - Phase A/PH_CURR
- U602 pad 1: /[6] 3-Phase Bridge - Phase B/PH_CURR -> /[6] 3-Phase Bridge - Phase B/PH_CIN+
- U602 pad 3: /[6] 3-Phase Bridge - Phase B/PH_CIN+ -> GND
- U602 pad 4: GND -> /[6] 3-Phase Bridge - Phase B/PH_CURR
- U702 pad 1: /[7] 3-Phase Bridge - Phase C/PH_CURR -> /[7] 3-Phase Bridge - Phase C/PH_CIN+
- U702 pad 3: /[7] 3-Phase Bridge - Phase C/PH_CIN+ -> GND
- U702 pad 4: GND -> /[7] 3-Phase Bridge - Phase C/PH_CURR
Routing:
- net (no net): track 187.1 -> 122.4 mm, vias 54 -> 40
- net /[7] 3-Phase Bridge - Phase C/PH_CIN+: track 61.9 -> 2.76 mm, vias 4 -> 1
- net /[7] 3-Phase Bridge - Phase C/PH_LOUT: track 29.2 -> 1.81 mm, vias 2 -> 0
- net /[7] 3-Phase Bridge - Phase C/PH_VS: track 42.5 -> 16.2 mm, vias 6 -> 2
- net /[7] 3-Phase Bridge - Phase C/PH_HOUT: track 26.2 -> 0.00 mm
- net /[2] MCU/PHA_VSDIV: track 8.82 -> 0.00 mm
- net /[2] MCU/PHC_VSDIV: track 8.82 -> 0.00 mm
- net /[7] 3-Phase Bridge - Phase C/PH_HOUT_G: track 7.61 -> 15.8 mm, vias 2 -> 0
- net GND: track 97.3 -> 89.9 mm, vias 81 -> 76
- net /[7] 3-Phase Bridge - Phase C/PH_CURR: track 5.54 -> 0.00 mm
- net +3.3VA: track 16.8 -> 12.3 mm, vias 8 -> 4
- net /[2] MCU/PHC_CURR_FILT: track 3.29 -> 0.00 mm
- net +BATT: track 12.0 -> 9.58 mm, vias 3 -> 17
- net /[7] 3-Phase Bridge - Phase C/PH_LOUT_G: track 9.44 -> 11.2 mm, vias 2 -> 0
- removed copper zone on F.Cu, net /[7] 3-Phase Bridge - Phase C/PH_CIN+
